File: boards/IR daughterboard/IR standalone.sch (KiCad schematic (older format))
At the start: 13 parts, among them J201 DB9, J202 DB9, U201 ISL83387E, U202 24AA014

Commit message: IR daughterboard done
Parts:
- removed J202: DB9, symbol DB9
- added K201: IR_RX, symbol CONN_3
- added K202: IR_TX, symbol CONN_3
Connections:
- net labels removed: C_CTS, C_DSR, C_DTR, C_RTS, C_RX, C_TX
- wire segments 90 -> 101
- no-connect marks 4 -> 9
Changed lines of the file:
@@
 $Descr A4 11693 8268
 encoding utf-8
-Sheet 2 2
+Sheet 2 3
 Title ""
 Date "26 jun 2014"
@@
 Text Label 2550 3650 2    60   ~ 0
 A_DSR
-Text Label 10100 3250 2    60   ~ 0
-C_DTR
-Text Label 10100 3350 2    60   ~ 0
-C_CTS
-Text Label 10100 3450 2    60   ~ 0
-C_TX
-Text Label 10100 3550 2    60   ~ 0
-C_RTS
-Text Label 10100 3650 2    60   ~ 0
-C_RX
-Text Label 10100 3750 2    60   ~ 0
-C_DSR
 Text Label 5350 3250 0    60   ~ 0
 B_RX
@@
 Text Label 5350 3750 0    60   ~ 0
 B_DTR
-Text Label 6300 3350 2    60   ~ 0
+Text Label 6950 3350 2    60   ~ 0
 B_RX
-Text Label 6300 3250 2    60   ~ 0
+Text Label 6950 3250 2    60   ~ 0
 B_TX
-Text Label 6300 3450 2    60   ~ 0
-B_RTS
-Text Label 6300 3550 2    60   ~ 0
-B_CTS
-Text Label 6300 3650 2    60   ~ 0
-B_DTR
-Text Label 6300 3750 2    60   ~ 0
-B_DSR
 Text Label 6000 2700 3    60   ~ 0
 B_RX
@@
 Text Label 5600 2700 3    60   ~ 0
 B_DSR
-NoConn ~ 10250 3850
-NoConn ~ 10250 3150
-$Comp
-L DB9 J202
-U 1 1 53ABD89D
-P 10700 3450
-F 0 "J202" H 10700 4000 70  0000 C CNN
-F 1 "DB9" H 10700 2900 70  0000 C CNN
-F 2 "" H 10700 3450 60  0000 C CNN
-F 3 "" H 10700 3450 60  0000 C CNN
-	1    10700 3450
-	1    0    0    -1
-$EndComp
 Wire Wire Line
 	4800 6450 4700 6450
@@
 	4700 6850 4700 7200
 Wire Wire Line
-	4550 7200 5500 7200
+	4550 7200 4700 7200
+Wire Wire Line
+	4700 7200 5500 7200
 Wire Wire Line
 	5500 7200 5500 7150
@@
 	5500 6050 5500 6150
 Wire Wire Line
-	6950 3250 6300 3250
-Wire Wire Line
-	6950 3350 6300 3350
-Wire Wire Line
-	6950 3450 6300 3450
-Wire Wire Line
-	6950 3550 6300 3550
-Wire Wire Line
-	6950 3650 6300 3650
-Wire Wire Line
-	6950 3750 6300 3750
+	7100 3250 6950 3250
+Wire Wire Line
+	7100 3350 6950 3350
 Wire Wire Line
 	2750 2650 2750 2600
 Wire Wire Line
-	2950 2350 2950 2750
+	2950 2350 2950 2600
+Wire Wire Line
+	2950 2600 2950 2700
+Wire Wire Line
+	2950 2700 2950 2750
 Connection ~ 2950 2700
 Wire Wire Line
-	2650 4150 3400 4150
+	2650 4150 2750 4150
+Wire Wire Line
+	2750 4150 2950 4150
+Wire Wire Line
+	2950 4150 3100 4150
+Wire Wire Line
+	3100 4150 3250 4150
+Wire Wire Line
+	3250 4150 3400 4150
 Wire Wire Line
 	2950 2950 2950 4150
@@
 	5450 4650 5450 4600
 Wire Wire Line
-	2750 2600 3400 2600
+	2750 2600 2950 2600
+Wire Wire Line
+	2950 2600 3400 2600
 Wire Wire Line
 	3250 2900 3400 2900
@@
 Wire Wire Line
 	5600 2350 5600 2700
-Wire Wire Line
-	10250 3650 10100 3650
-Wire Wire Line
-	10250 3250 10100 3250
-Wire Wire Line
-	10250 3350 10100 3350
-Wire Wire Line
-	10250 3750 10100 3750
-Wire Wire Line
-	10250 3450 10100 3450
-Wire Wire Line
-	10250 3550 10100 3550
 $Comp
 L PWR_FLAG #FLG201
@@
 Wire Wire Line
 	1700 3150 1700 3000
-Wire Wire Line
-	10250 3050 10100 3050
-Text HLabel 10100 2900 1    60   Input ~ 0
-GND_ISO
-Wire Wire Line
-	10100 3050 10100 2900
 $Comp
 L R R203
@@
 Wire Wire Line
 	4800 6050 4700 6050
+Wire Wire Line
+	7100 3100 6950 3100
+Text Label 6950 3100 2    60   ~ 0
+VCC_5V_ISO
+Wire Wire Line
+	7100 3500 6950 3500
+Text Label 6950 3500 2    60   ~ 0
+GND_ISO
+Wire Wire Line
+	8300 3100 7950 3100
+Wire Wire Line
+	8300 3200 7950 3200
+Wire Wire Line
+	8300 3300 7950 3300
+Wire Wire Line
+	9250 3400 7950 3400
+Wire Wire Line
+	7950 3500 8550 3500
+Wire Wire Line
+	8300 3600 7950 3600
+Wire Wire Line
+	8300 3700 7950 3700
+Wire Wire Line
+	8300 3800 7950 3800
+Text Label 9100 3500 2    60   ~ 0
+VCC_5V_ISO
+Text Label 9100 3600 2    60   ~ 0
+GND_ISO
+$Sheet
+S 7100 3000 850  900
+U 53AC80BA
+F0 "PIC-GPIO8.sch" 50
+F1 "PIC-GPIO8.sch" 50
+F2 "VCC" I L 7100 3100 60
+F3 "GND" I L 7100 3500 60
+F4 "GPIO0" B R 7950 3100 60
+F5 "GPIO1" B R 7950 3200 60
+F6 "GPIO2" B R 7950 3300 60
+F7 "GPIO5" B R 7950 3600 60
+F8 "GPIO6" B R 7950 3700 60
+F9 "GPIO7" B R 7950 3800 60
+F10 "GPIO4" B R 7950 3500 60
+F11 "GPIO3" B R 7950 3400 60
+F12 "RX" I L 7100 3350 60
+F13 "TX" O L 7100 3250 60
+$EndSheet
+$Comp
+L CONN_3 K201
+U 1 1 53AC99B7
+P 9600 3500
+F 0 "K201" V 9550 3500 50  0000 C CNN
+F 1 "IR_RX" V 9650 3500 40  0000 C CNN
+F 2 "" H 9600 3500 60  0000 C CNN
+F 3 "" H 9600 3500 60  0000 C CNN
+	1    9600 3500
+	1    0    0    -1
+$EndComp
+$Comp
+L CONN_3 K202
+U 1 1 53AC9D39
+P 9600 3900
+F 0 "K202" V 9550 3900 50  0000 C CNN
+F 1 "IR_TX" V 9650 3900 40  0000 C CNN
+F 2 "" H 9600 3900 60  0000 C CNN
+F 3 "" H 9600 3900 60  0000 C CNN
+	1    9600 3900
+	1    0    0    -1
+$EndComp
+Wire Wire Line
+	8550 3500 8550 3800
+Wire Wire Line
+	8550 3800 9250 3800
+Wire Wire Line
+	9100 3500 9250 3500
+Wire Wire Line
+	9250 3600 9100 3600
+Text Label 9100 4000 2    60   ~ 0
+GND_ISO
+Wire Wire Line
+	9250 4000 9100 4000
+NoConn ~ 9250 3900
+NoConn ~ 8300 3100
+NoConn ~ 8300 3200
+NoConn ~ 8300 3300
+NoConn ~ 8300 3600
+NoConn ~ 8300 3700
+NoConn ~ 8300 3800
 $EndSCHEMATC

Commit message: Updated IR dboard to use RS232 adapter block; Changed power hierarchy pins in RS232 adapter block and GPIO 8 sheet as passive type
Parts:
- removed C201, C202, C203, C204, C205, C206: 0.1u, ~, symbol CSMALL
- removed D201: LED, ~, symbol LED
- removed J201: DB9, symbol DB9
- removed R201: R, ~, symbol R
- removed U201: ISL83387E, ~, symbol ISL83387E
- renumbered R203 to R201, U202 to U201
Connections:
- net labels removed: A_CTS, A_DSR, A_DTR, A_RTS, A_RX, A_TX, B_CTS, B_DSR, B_DTR, B_RTS
- wire segments 101 -> 49
- no-connect marks 9 -> 15

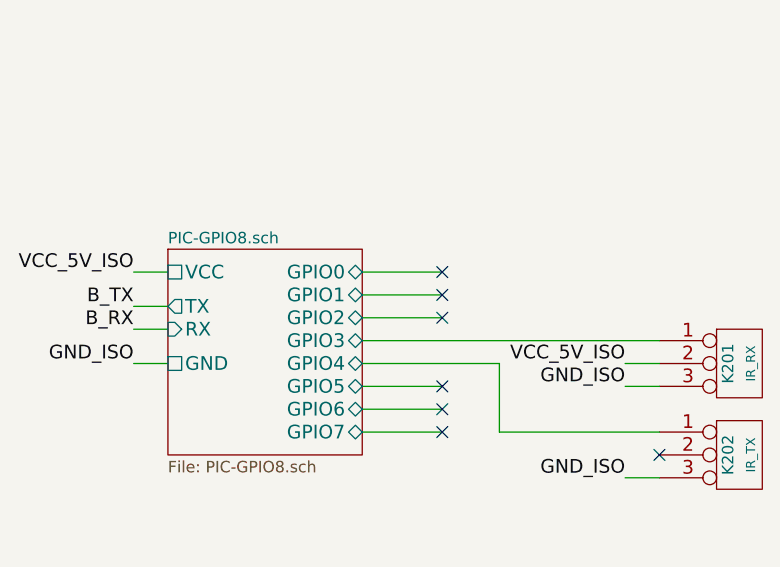
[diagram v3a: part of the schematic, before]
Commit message: Updated IR dboard to use RS232 adapter block; Changed power hierarchy pins in RS232 adapter block and GPIO 8 sheet as passive type; Reannotated sheet
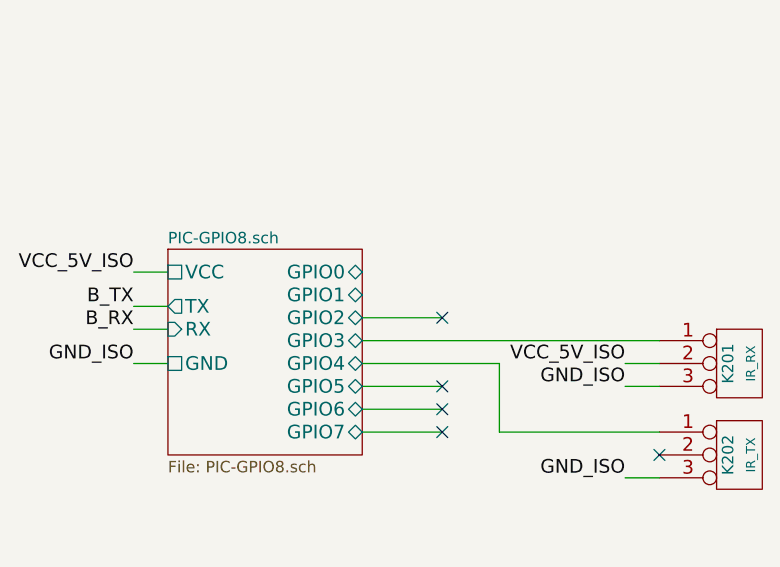
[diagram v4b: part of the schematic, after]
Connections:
- no-connect marks 15 -> 13
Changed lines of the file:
@@
 GND_ISO
-Wire Wire Line
-	8300 3100 7950 3100
-Wire Wire Line
-	8300 3200 7950 3200
 Wire Wire Line
 	8300 3300 7950 3300
@@
 Text HLabel 3500 3300 0    60   UnSpc ~ 0
 GND_ISO
-NoConn ~ 8300 3200
-NoConn ~ 8300 3100
 Wire Wire Line
 	8550 6200 8400 6200
@@
 VCC_5V_ISO
 $Comp
-L PWR_FLAG #FLG?
+L PWR_FLAG #FLG04
 U 1 1 53B298D3
 P 8550 6050
-F 0 "#FLG?" H 8550 6145 30  0001 C CNN
+F 0 "#FLG04" H 8550 6145 30  0001 C CNN
 F 1 "PWR_FLAG" H 8550 6230 30  0001 C CNN
 F 2 "" H 8550 6050 60  0000 C CNN
